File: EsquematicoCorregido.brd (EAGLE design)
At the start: 70.9 x 80 mm, 45 parts, among them IC1 OPA991TIDCKR, IC10 MCP73831T-2ACI_OT, IC2 AD8226ARZ-RL, IC3 OPA991TIDCKR, IC4 ESP32-S3-WROOM-1-N16R8, IC5 OPA991TIDCKR, IC6 MAX30102EFD+T, IC7 LP38692MP-3.3_NOPB, IC8 LP38692MP-1.8_NOPB, IC9 REF2033AIDDCT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

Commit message: pines de tierra GND
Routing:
- net GND: vias 24 -> 25
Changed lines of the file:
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@@
 <via x="30.48" y="26.67" extent="1-16" drill="0.35"/>
 <via x="35.56" y="25.4" extent="1-16" drill="0.35"/>
+<via x="6.35" y="48.26" extent="1-16" drill="0.35"/>
 <wire x1="35.1" y1="61.54" x2="22.987" y2="63.82" width="0" layer="19" extent="1-1"/>
 <wire x1="36.37" y1="75.51" x2="35.1" y2="61.54" width="0" layer="19" extent="1-1"/>

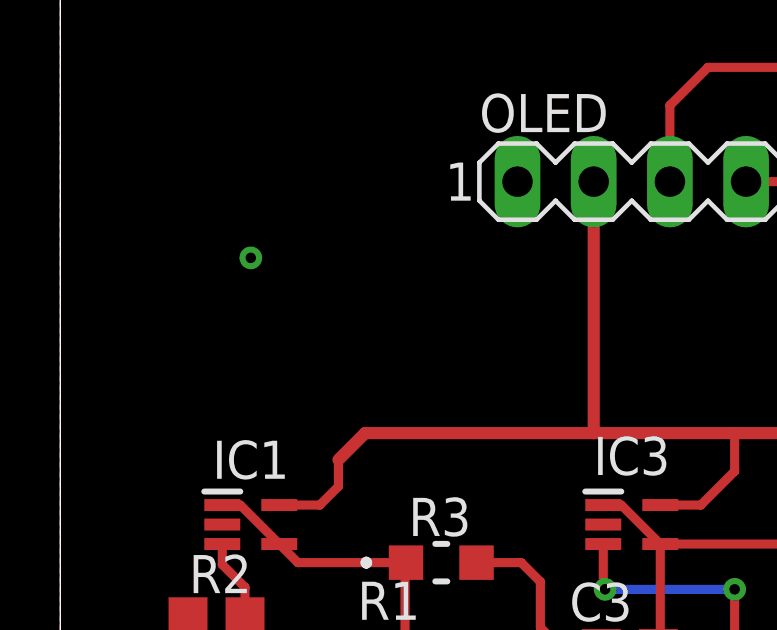
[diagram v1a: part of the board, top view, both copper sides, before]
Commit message: tierras de la PCB
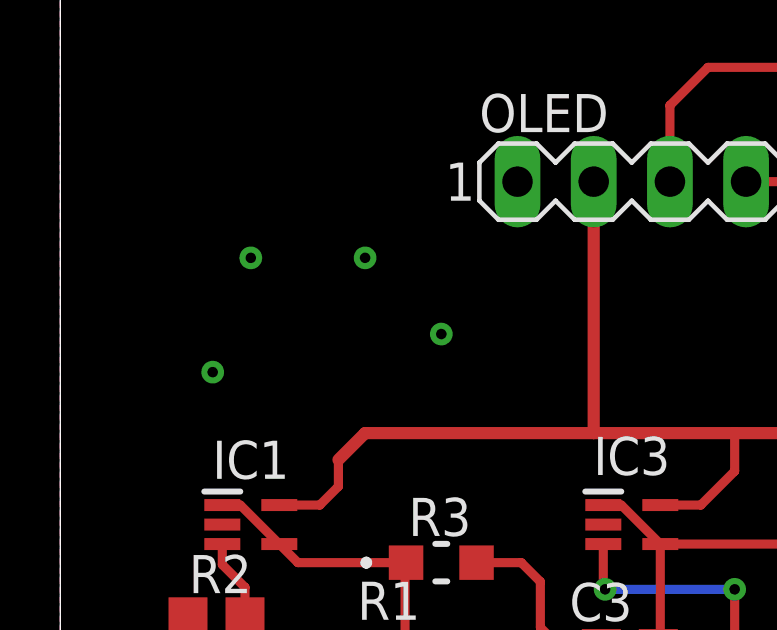
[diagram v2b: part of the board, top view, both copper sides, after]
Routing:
- net GND: vias 25 -> 26
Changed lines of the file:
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@@
 <via x="35.56" y="25.4" extent="1-16" drill="0.35"/>
 <via x="6.35" y="48.26" extent="1-16" drill="0.35"/>
+<via x="12.7" y="45.72" extent="1-16" drill="0.35"/>
 <wire x1="35.1" y1="61.54" x2="22.987" y2="63.82" width="0" layer="19" extent="1-1"/>
 <wire x1="36.37" y1="75.51" x2="35.1" y2="61.54" width="0" layer="19" extent="1-1"/>
@@
 <wire x1="54.356" y1="27.686" x2="50.419" y2="27.686" width="0.3048" layer="1"/>
 </signal>
+<signal name="N$10">
+<via x="10.16" y="48.26" extent="1-16" drill="0.35"/>
+</signal>
+<signal name="N$15">
+<via x="5.08" y="44.45" extent="1-16" drill="0.35"/>
+</signal>
 </signals>
